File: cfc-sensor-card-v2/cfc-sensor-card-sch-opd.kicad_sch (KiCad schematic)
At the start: 71 parts, among them Q1 DMP2240UDM, Q2 PMV45EN, Q3 DMP3050LVT-7, Q4 DMP3050LVT-7, Q5 PMV45EN, U1 MIC842LYC5, U2 MIC842LYC5, U3 MAX7310ATE+, U4 MAX4211FETE

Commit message: Update
updated opd address resistors to 100 ohms from 100 ohms, changed the 100 ohm res VBUSP to 10 ohms. Updated TEC page for sensor to have bidirectional current sense for diag. Removed misc testpoints
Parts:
- removed TP6, TP7: TestPoint-MinTH, oresat-misc:TestPoint_Pad_D1.0mm, symbol oresat-misc:Test-Point-1mm-round
- Q2, Q5: footprint Package_TO_SOT_SMD:SOT-23-3 -> Package_TO_SOT_SMD:SOT-23
- R11: value 100 -> 10; DPN RMCF0603FT100RCT-ND -> RMCF0603FT10R0CT-ND; MPN RMCF0603FT100R -> RMCF0603FT10R0
- R21, R4, R8: value 1k -> 100; DPN RMCF0603FT1K00CT-ND -> RMCF0603FT100RCT-ND; MPN RMCF0603FT1K00 -> RMCF0603FT100R
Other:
- note added: ""ON""
- note added: ""VBUSP""

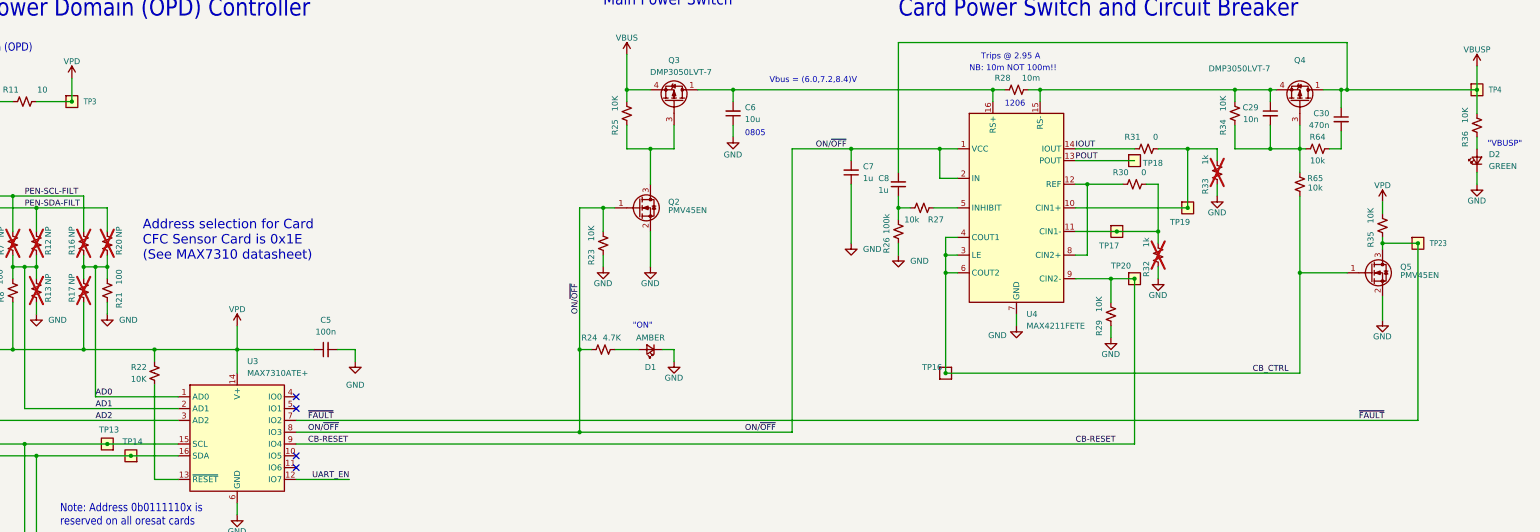
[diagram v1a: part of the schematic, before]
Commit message: Processor board routing
Completed rework and routing of processor board. No drc errors or warnings. Ready for design review on processor board. Minor changes to schematic for easier routing on pull down resistors connected to the octavo SIP. Reannotated sensor schematic component designators.
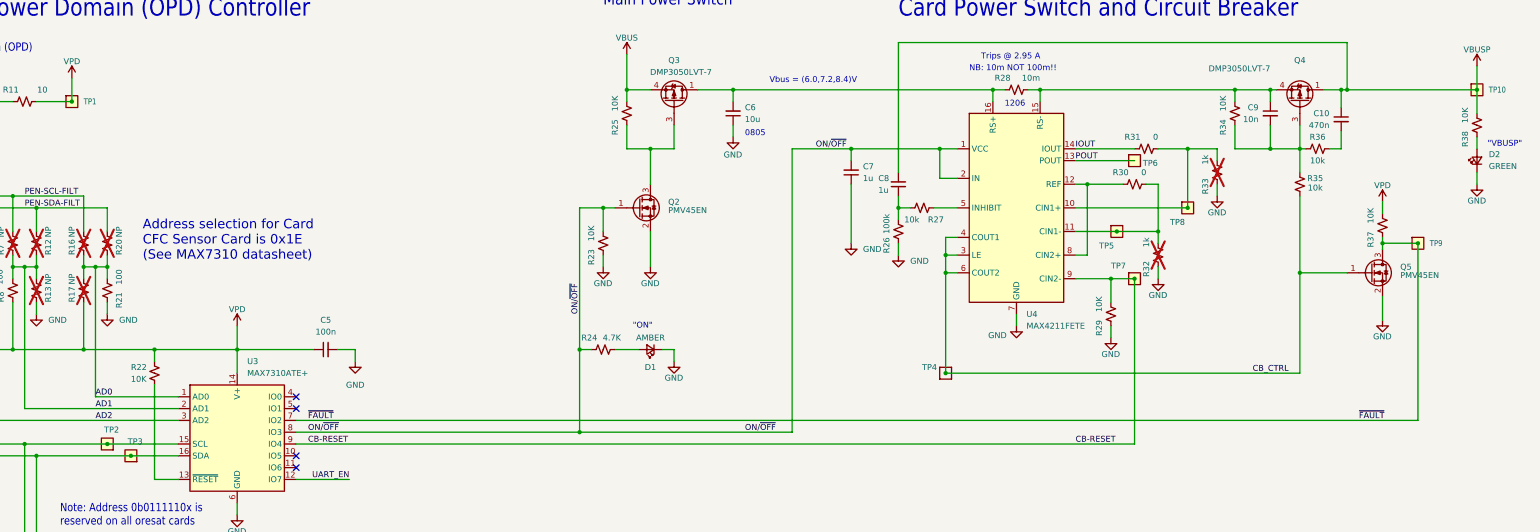
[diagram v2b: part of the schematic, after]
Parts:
- renumbered C30 to C10, C29 to C9, R65 to R35, R64 to R36, R35 to R37, R36 to R38, TP3 to TP1, TP4 to TP10, TP13 to TP2, TP14 to TP3, TP16 to TP4, TP17 to TP5, TP18 to TP6, TP20 to TP7, TP19 to TP8, TP23 to TP9

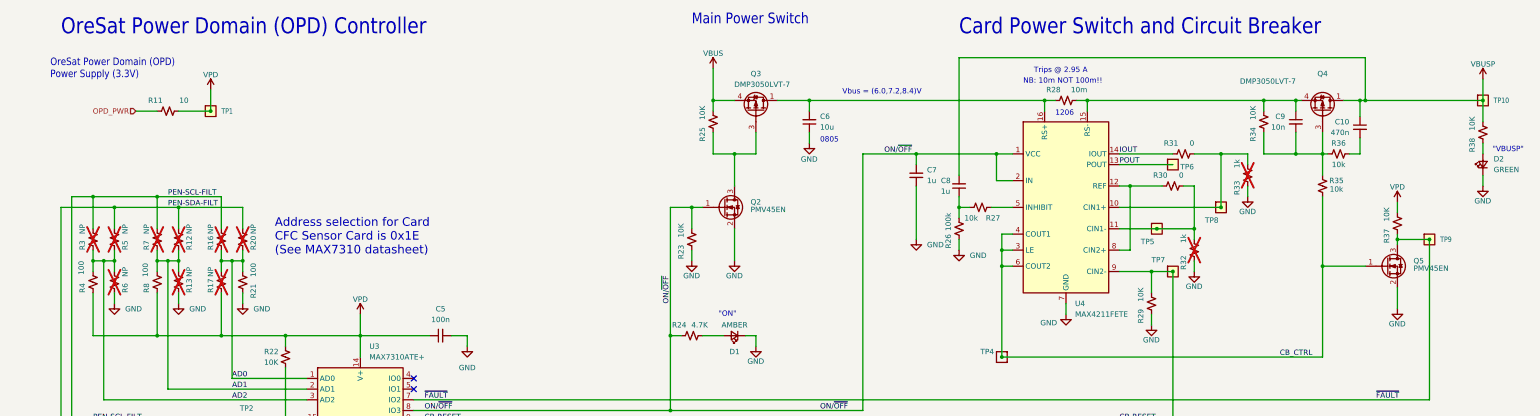
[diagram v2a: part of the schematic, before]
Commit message: Updated OPD on sensor card
updated OPD on sensor card to match protocard. Finished placement on PCB.
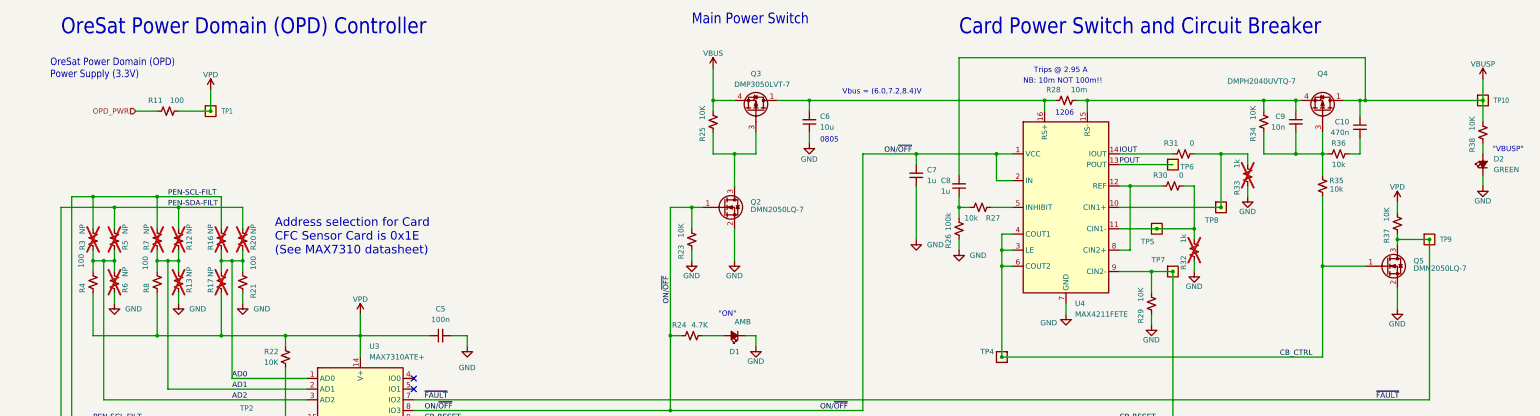
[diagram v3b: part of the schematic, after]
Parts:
- D1: value AMBER -> AMB; symbol Device:LED_Small -> Device:LED_Small_Filled
- D2: symbol Device:LED_Small -> Device:LED_Small_Filled
- Q2, Q5: value PMV45EN -> DMN2050LQ-7; DPN 1727-2307-1-ND -> 31-DMN2050LQ-7CT-ND; MFR Nexperia -> Diodes Incorporated; MPN PMV45EN2R -> DMN2050LQ-7
- Q4: value DMP3050LVT-7 -> DMPH2040UVTQ-7; DPN DMP3050LVT-7DICT-ND -> 31-DMPH2040UVTQ-7CT-ND; MFR Diodes Inc -> Diodes Incorporated; MPN DMP3050LVT-7 -> DMPH2040UVTQ-7
- R11: value 10 -> 100; DPN RMCF0603FT10R0CT-ND -> RMCF0603FT100RCT-ND; MPN RMCF0603FT10R0 -> RMCF0603FT100R
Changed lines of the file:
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@@
 			)
 		)
-		(property "Value" "10"
+		(property "Value" "100"
 			(at 67.31 43.18 90)
 			(show_name no)
@@
 					(size 1.27 1.27)
 				)
+				(justify left)
 			)
 		)
@@
 			)
 		)
-		(property "Datasheet" "https://www.seielect.com/catalog/SEI-RMCF_RMCP.pdf"
+		(property "Datasheet" "https://www.seielect.com/catalog/sei-rmcf_rmcp.pdf"
 			(at 63.5 45.72 0)
 			(hide yes)
@@
 			)
 		)
-		(property "Description" "10 Ohms ±1% 0.1W, 1/10W Chip Resistor 0603 (1608 Metric) Automotive AEC-Q200 Thick Film"
+		(property "Description" "100 Ohms ±1% 0.1W, 1/10W Chip Resistor 0603 (1608 Metric) Automotive AEC-Q200 Thick Film"
 			(at 63.5 45.72 0)
 			(hide yes)
@@
 					(size 1.27 1.27)
 				)
-				(justify right top)
 			)
 		)
-		(property "DPN" "RMCF0603FT10R0CT-ND"
+		(property "DPN" "RMCF0603FT100RCT-ND"
 			(at 63.5 45.72 90)
 			(hide yes)
@@
 					(size 1.27 1.27)
 				)
-				(justify right top)
 			)
 		)
@@
 					(size 1.27 1.27)
 				)
-				(justify right top)
 			)
 		)
-		(property "MPN" "RMCF0603FT10R0"
+		(property "MPN" "RMCF0603FT100R"
 			(at 63.5 45.72 90)
 			(hide yes)
@@
 					(size 1.27 1.27)
 				)
-				(justify right top)
 			)
 		)
@@
 	)
 	(symbol
-		(lib_id "Device:LED_Small")
+		(lib_id "Device:LED_Small_Filled")
 		(at 375.92 58.42 90)
 		(unit 1)
@@
 			)
 		)
-		(property "Description" "Light emitting diode, small symbol"
+		(property "Description" "Light emitting diode, small symbol, filled shape"
 			(at 375.92 58.42 0)
 			(hide yes)
@@
 					(size 1.27 1.27)
 				)
-				(justify right)
 			)
 		)
@@
 			)
 		)
-		(property "Datasheet" "https://www.seielect.com/catalog/sei-rmcf_rmcp.pdf"
+		(property "Datasheet" "https://www.seielect.com/catalog/SEI-RMCF_RMCP.pdf"
 			(at 45.72 86.36 0)
 			(hide yes)
@@
 					(size 1.27 1.27)
 				)
+				(justify right top)
 			)
 		)
@@
 					(size 1.27 1.27)
 				)
+				(justify right top)
 			)
 		)
@@
 					(size 1.27 1.27)
 				)
+				(justify right top)
 			)
 		)
@@
 					(size 1.27 1.27)
 				)
+				(justify right top)
 			)
 		)
@@
 			)
 		)
-		(property "Value" "DMP3050LVT-7"
+		(property "Value" "DMPH2040UVTQ-7"
 			(at 331.47 39.37 90)
 			(show_name no)
@@
 			)
 		)
-		(property "Datasheet" "https://www.diodes.com/assets/Datasheets/DMP3050LVT.pdf"
+		(property "Datasheet" "https://www.diodes.com/assets/Datasheets/DMPH2040UVTQ.pdf"
 			(at 337.82 45.72 90)
 			(hide yes)
@@
 			)
 		)
-		(property "Description" "P-Channel Power MOSFET, TSOT-23-6"
+		(property "Description" "P-Channel 20 V 5.6A (Ta), 11.7A (Tc) 1W (Ta) Surface Mount TSOT-26"
 			(at 337.82 45.72 0)
 			(hide yes)
@@
 			)
 		)
-		(property "DPN" "DMP3050LVT-7DICT-ND"
+		(property "DPN" "31-DMPH2040UVTQ-7CT-ND"
 			(at 337.82 45.72 90)
 			(hide yes)
@@
 			)
 		)
-		(property "MFR" "Diodes Inc"
+		(property "MFR" "Diodes Incorporated"
 			(at 337.82 45.72 90)
 			(hide yes)
@@
 			)
 		)
-		(property "MPN" "DMP3050LVT-7"
+		(property "MPN" "DMPH2040UVTQ-7"
 			(at 337.82 45.72 90)
 			(hide yes)
@@
 			)
 		)
-		(property "Value" "PMV45EN"
+		(property "Value" "DMN2050LQ-7"
 			(at 359.41 83.8199 0)
 			(show_name no)
@@
 			)
 		)
-		(property "Datasheet" "https://assets.nexperia.com/documents/data-sheet/PMV45EN2.pdf"
+		(property "Datasheet" "https://www.diodes.com/datasheet/download/DMN2050LQ.pdf"
 			(at 353.06 82.55 0)
 			(hide yes)
@@
 			)
 		)
-		(property "Description" "N-Channel 30 V 4.1A (Ta) 510mW (Ta), 5W (Tc) Surface Mount TO-236AB"
+		(property "Description" "N-Channel 20 V 5.9A (Ta) 1.4W Surface Mount SOT-23-3"
 			(at 353.06 82.55 0)
 			(hide yes)
@@
 			)
 		)
-		(property "DPN" "1727-2307-1-ND"
+		(property "DPN" "31-DMN2050LQ-7CT-ND"
 			(at 353.06 82.55 0)
 			(hide yes)
@@
 			)
 		)
-		(property "MFR" "Nexperia"
+		(property "MFR" "Diodes Incorporated"
 			(at 353.06 82.55 0)
 			(hide yes)
@@
 			)
 		)
-		(property "MPN" "PMV45EN2R"
+		(property "MPN" "DMN2050LQ-7"
 			(at 353.06 82.55 0)
 			(hide yes)
@@
 					(size 1.27 1.27)
 				)
-				(justify right)
 			)
 		)
@@
 			)
 		)
-		(property "Datasheet" "https://www.seielect.com/catalog/sei-rmcf_rmcp.pdf"
+		(property "Datasheet" "https://www.seielect.com/catalog/SEI-RMCF_RMCP.pdf"
 			(at 81.28 86.36 0)
 			(hide yes)
@@
 					(size 1.27 1.27)
 				)
+				(justify right top)
 			)
 		)
@@
 					(size 1.27 1.27)
 				)
+				(justify right top)
 			)
 		)
@@
 					(size 1.27 1.27)
 				)
+				(justify right top)
 			)
 		)
@@
 					(size 1.27 1.27)
 				)
+				(justify right top)
 			)
 		)
@@
 					(size 1.27 1.27)
 				)
-				(justify right)
 			)
 		)
@@
 			)
 		)
-		(property "Datasheet" "https://www.seielect.com/catalog/sei-rmcf_rmcp.pdf"
+		(property "Datasheet" "https://www.seielect.com/catalog/SEI-RMCF_RMCP.pdf"
 			(at 60.96 86.36 0)
 			(hide yes)
@@
 					(size 1.27 1.27)
 				)
+				(justify right top)
 			)
 		)
@@
 					(size 1.27 1.27)
 				)
+				(justify right top)
 			)
 		)
@@
 					(size 1.27 1.27)
 				)
+				(justify right top)
 			)
 		)
@@
 					(size 1.27 1.27)
 				)
+				(justify right top)
 			)
 		)
@@
 	)
 	(symbol
-		(lib_name "LED_Small_1")
-		(lib_id "Device:LED_Small")
+		(lib_id "Device:LED_Small_Filled")
 		(at 198.12 99.06 180)
 		(unit 1)
@@
 			)
 		)
-		(property "Value" "AMBER"
+		(property "Value" "AMB"
 			(at 198.12 96.52 0)
 			(show_name no)
@@
 					(size 1.27 1.27)
 				)
+				(justify right top)
 			)
 		)
@@
 			)
 		)
-		(property "Datasheet" "https://www.we-online.com/components/products/datasheet/150060AS75000.pdf"
+		(property "Datasheet" "https://www.we-online.com/catalog/datasheet/150060AS75000.pdf"
 			(at 198.12 99.06 90)
 			(hide yes)
@@
 			)
 		)
-		(property "Description" "Light emitting diode, small symbol"
+		(property "Description" "Light emitting diode, small symbol, filled shape"
 			(at 198.12 99.06 0)
 			(hide yes)
@@
 			)
 		)
-		(property "Sim.Pin" "1=K 2=A"
+		(property "DIS" "DigiKey"
 			(at 198.12 99.06 0)
 			(hide yes)
@@
 					(size 1.27 1.27)
 				)
+				(justify right bottom)
 			)
 		)
-		(property "DIS" "DigiKey"
+		(property "DPN" "732-150060AS75000CT-ND"
 			(at 198.12 99.06 0)
 			(hide yes)
@@
 					(size 1.27 1.27)
 				)
+				(justify right bottom)
 			)
 		)
-		(property "DPN" "732-150060AS75000CT-ND"
+		(property "MFR" "Wurth"
 			(at 198.12 99.06 0)
 			(hide yes)
@@
 					(size 1.27 1.27)
 				)
+				(justify right bottom)
 			)
 		)
-		(property "MFR" "Wurth"
+		(property "MPN" "150060AS75000"
 			(at 198.12 99.06 0)
 			(hide yes)
@@
 					(size 1.27 1.27)
 				)
+				(justify right bottom)
 			)
 		)
-		(property "MPN" "150060AS75000"
+		(property "Sim.Device" "D"
 			(at 198.12 99.06 0)
 			(hide yes)
@@
 			)
 		)
-		(property "Value" "PMV45EN"
+		(property "Value" "DMN2050LQ-7"
 			(at 201.93 69.8499 0)
 			(show_name no)
@@
 			)
 		)
-		(property "Datasheet" "https://assets.nexperia.com/documents/data-sheet/PMV45EN2.pdf"
+		(property "Datasheet" "https://www.diodes.com/datasheet/download/DMN2050LQ.pdf"
 			(at 195.58 68.58 0)
 			(hide yes)
@@
 			)
 		)
-		(property "Description" "N-Channel 30 V 4.1A (Ta) 510mW (Ta), 5W (Tc) Surface Mount TO-236AB"
+		(property "Description" "N-Channel 20 V 5.9A (Ta) 1.4W Surface Mount SOT-23-3"
 			(at 195.58 68.58 0)
 			(hide yes)
@@
 			)
 		)
-		(property "DPN" "1727-2307-1-ND"
+		(property "DPN" "31-DMN2050LQ-7CT-ND"
 			(at 195.58 68.58 0)
 			(hide yes)
@@
 			)
 		)
-		(property "MFR" "Nexperia"
+		(property "MFR" "Diodes Incorporated"
 			(at 195.58 68.58 0)
 			(hide yes)
@@
 			)
 		)
-		(property "MPN" "PMV45EN2R"
+		(property "MPN" "DMN2050LQ-7"
 			(at 195.58 68.58 0)
 			(hide yes)
@@
 					(size 1.27 1.27)
 				)
-				(justify left)
+				(justify left bottom)
 			)
 		)

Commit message: Update
Fixed all DRC errors and warnings.
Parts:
- R3, R7: footprint Resistor_SMD:R_0603_1608Metric_Pad0.98x0.95mm_HandSolder -> oresat-passives:0603-C-NOSILK
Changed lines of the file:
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@@
 			)
 		)
-		(property "Footprint" "Resistor_SMD:R_0603_1608Metric_Pad0.98x0.95mm_HandSolder"
+		(property "Footprint" "oresat-passives:0603-C-NOSILK"
 			(at 45.72 76.2 0)
 			(hide yes)
@@
 			)
 		)
-		(property "Description" ""
+		(property "Description" "Resistor, small US symbol"
 			(at 45.72 76.2 0)
 			(hide yes)
@@
 			)
 		)
-		(property "Description" ""
+		(property "Description" "Resistor, small US symbol"
 			(at 50.8 76.2 0)
 			(hide yes)
@@
 			)
 		)
-		(property "Description" ""
+		(property "Description" "Resistor, small US symbol"
 			(at 66.04 86.36 0)
 			(hide yes)
@@
 			)
 		)
-		(property "Description" ""
+		(property "Description" "Resistor, small US symbol"
 			(at 50.8 86.36 0)
 			(hide yes)
@@
 			)
 		)
-		(property "Description" ""
+		(property "Description" "Resistor, small US symbol"
 			(at 76.2 76.2 0)
 			(hide yes)
@@
 			)
 		)
-		(property "Description" ""
+		(property "Description" "Resistor, small US symbol"
 			(at 66.04 76.2 0)
 			(hide yes)
@@
 			)
 		)
-		(property "Description" ""
+		(property "Description" "Resistor, small US symbol"
 			(at 76.2 86.36 0)
 			(hide yes)
@@
 			)
 		)
-		(property "Footprint" "Resistor_SMD:R_0603_1608Metric_Pad0.98x0.95mm_HandSolder"
+		(property "Footprint" "oresat-passives:0603-C-NOSILK"
 			(at 60.96 76.2 0)
 			(hide yes)
@@
 			)
 		)
-		(property "Description" ""
+		(property "Description" "Resistor, small US symbol"
 			(at 60.96 76.2 0)
 			(hide yes)
@@
 			)
 		)
-		(property "Description" ""
+		(property "Description" "Resistor, small US symbol"
 			(at 81.28 76.2 0)
 			(hide yes)
